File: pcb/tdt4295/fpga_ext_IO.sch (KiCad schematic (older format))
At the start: 44 parts, among them J301 618015330923, J302 Conn_02x08_Odd_Even, U301 NUP4114UCW1T2G, U302 NUP4114UCW1T2G, U303 NUP4114UCW1T2G, U304 NUP4114UCW1T2G

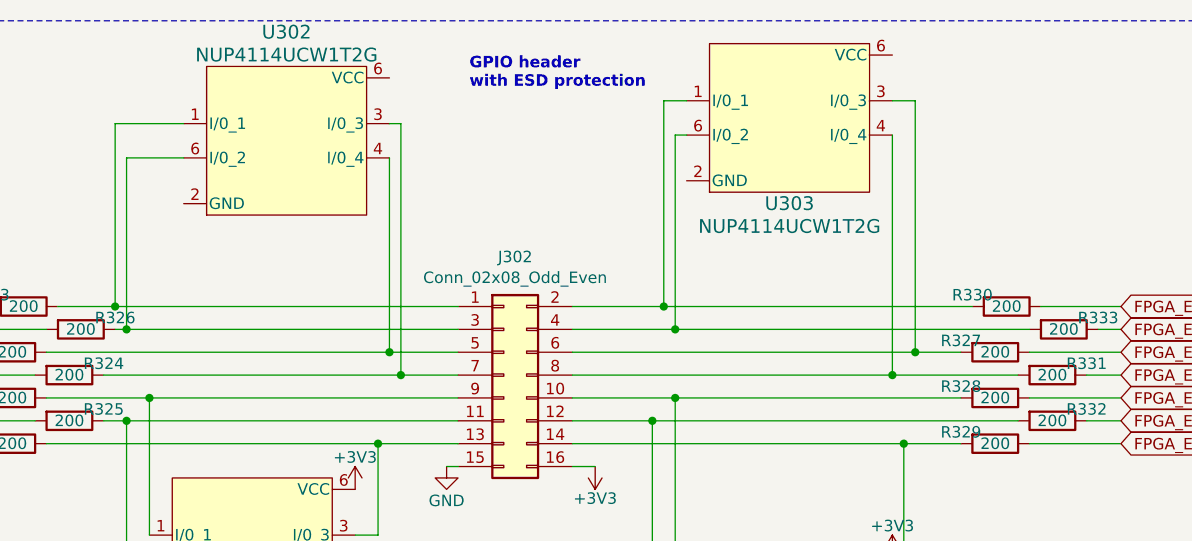
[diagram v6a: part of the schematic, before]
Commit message: correct errors spotted by Markus
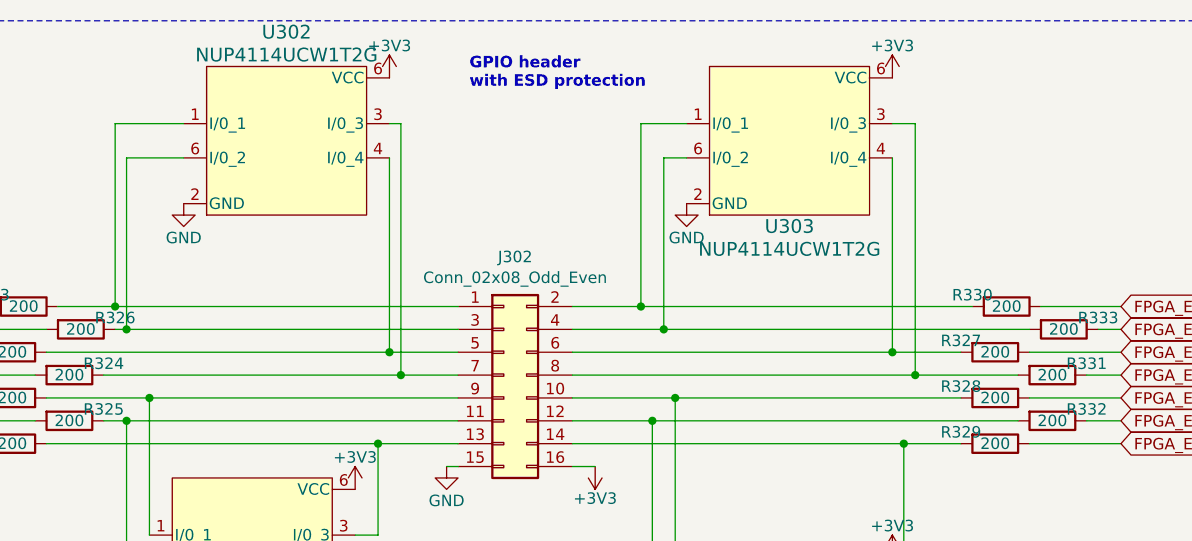
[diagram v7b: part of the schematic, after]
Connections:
- net +3V3: now also U302.6 (VCC), U303.6 (VCC)
- net GND: now also U302.2 (GND), U303.2 (GND)
- net at J302.6 (Pin_6), R327.2: now also U303.4 (I/0_4); no longer U303.3 (I/0_3)
- net at J302.8 (Pin_8), R331.2: now also U303.3 (I/0_3); no longer U303.4 (I/0_4)
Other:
- moved on the sheet: U303
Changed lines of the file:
@@
 L NUP4114UCW1T2G:NUP4114UCW1T2G U303
 U 1 1 61BB530D
-P 8000 1000
-F 0 "U303" H 8000 700 60  0000 C CNN
-F 1 "NUP4114UCW1T2G" H 8000 600 60  0000 C CNN
-F 2 "NUP4114UCW1T2G-footprint:NUP4114UCW1T2G" H 8000 490 60  0001 C CNN
-F 3 "https://www.onsemi.com/pdf/datasheet/nup4114-d.pdf" H 7200 -450 60  0001 C CNN
-	1    8000 1000
-	1    0    0    -1
-$EndComp
-Wire Wire Line
-	7050 1750 7450 1750
-Wire Wire Line
-	7050 1850 7500 1850
-Wire Wire Line
-	7550 850  7450 850
-Wire Wire Line
-	7450 850  7450 1750
-Connection ~ 7450 1750
-Wire Wire Line
-	7450 1750 8800 1750
-Wire Wire Line
-	7550 1000 7500 1000
-Wire Wire Line
-	7500 1000 7500 1850
-Connection ~ 7500 1850
-Wire Wire Line
-	7500 1850 9050 1850
-Wire Wire Line
-	8450 850  8550 850
-Wire Wire Line
-	8550 850  8550 1950
-Wire Wire Line
-	8450 1000 8450 2050
-Wire Wire Line
-	7050 2050 8450 2050
-Connection ~ 8450 2050
-Wire Wire Line
-	8450 2050 9000 2050
-Wire Wire Line
-	7050 1950 8550 1950
-Connection ~ 8550 1950
-Wire Wire Line
-	8550 1950 8750 1950
+P 8000 1100
+F 0 "U303" H 8000 800 60  0000 C CNN
+F 1 "NUP4114UCW1T2G" H 8000 700 60  0000 C CNN
+F 2 "NUP4114UCW1T2G-footprint:NUP4114UCW1T2G" H 8000 590 60  0001 C CNN
+F 3 "https://www.onsemi.com/pdf/datasheet/nup4114-d.pdf" H 7200 -350 60  0001 C CNN
+	1    8000 1100
+	1    0    0    -1
+$EndComp
+Wire Wire Line
+	8450 950  8550 950
 Wire Wire Line
 	7050 2150 7500 2150
@@
 NoConn ~ 8450 3200
 NoConn ~ 6100 2900
+$Comp
+L power:GND #PWR?
+U 1 1 61500DE1
+P 7550 1300
+F 0 "#PWR?" H 7550 1050 50  0001 C CNN
+F 1 "GND" H 7550 1150 50  0000 C CNN
+F 2 "" H 7550 1300 50  0001 C CNN
+F 3 "" H 7550 1300 50  0001 C CNN
+	1    7550 1300
+	1    0    0    -1
+$EndComp
+$Comp
+L power:GND #PWR?
+U 1 1 61501C42
+P 5350 1300
+F 0 "#PWR?" H 5350 1050 50  0001 C CNN
+F 1 "GND" H 5350 1150 50  0000 C CNN
+F 2 "" H 5350 1300 50  0001 C CNN
+F 3 "" H 5350 1300 50  0001 C CNN
+	1    5350 1300
+	1    0    0    -1
+$EndComp
+$Comp
+L power:+3V3 #PWR?
+U 1 1 615023D2
+P 6250 750
+F 0 "#PWR?" H 6250 600 50  0001 C CNN
+F 1 "+3V3" H 6250 890 50  0000 C CNN
+F 2 "" H 6250 750 50  0001 C CNN
+F 3 "" H 6250 750 50  0001 C CNN
+	1    6250 750
+	1    0    0    -1
+$EndComp
+$Comp
+L power:+3V3 #PWR?
+U 1 1 61502D32
+P 8450 750
+F 0 "#PWR?" H 8450 600 50  0001 C CNN
+F 1 "+3V3" H 8450 890 50  0000 C CNN
+F 2 "" H 8450 750 50  0001 C CNN
+F 3 "" H 8450 750 50  0001 C CNN
+	1    8450 750
+	1    0    0    -1
+$EndComp
+Wire Wire Line
+	7050 1750 7350 1750
+Wire Wire Line
+	7050 1850 7450 1850
+Wire Wire Line
+	7050 1950 8450 1950
+Wire Wire Line
+	7050 2050 8550 2050
+Wire Wire Line
+	7450 1100 7450 1850
+Wire Wire Line
+	7450 1100 7550 1100
+Connection ~ 7450 1850
+Wire Wire Line
+	7450 1850 9050 1850
+Wire Wire Line
+	7350 950  7350 1750
+Wire Wire Line
+	7350 950  7550 950
+Connection ~ 7350 1750
+Wire Wire Line
+	7350 1750 8800 1750
+Wire Wire Line
+	8450 1100 8450 1950
+Connection ~ 8450 1950
+Wire Wire Line
+	8450 1950 8750 1950
+Wire Wire Line
+	8550 950  8550 2050
+Connection ~ 8550 2050
+Wire Wire Line
+	8550 2050 9000 2050
 $EndSCHEMATC
